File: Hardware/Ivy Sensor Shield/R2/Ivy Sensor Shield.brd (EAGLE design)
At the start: 47.1 x 37.5 mm, 16 parts

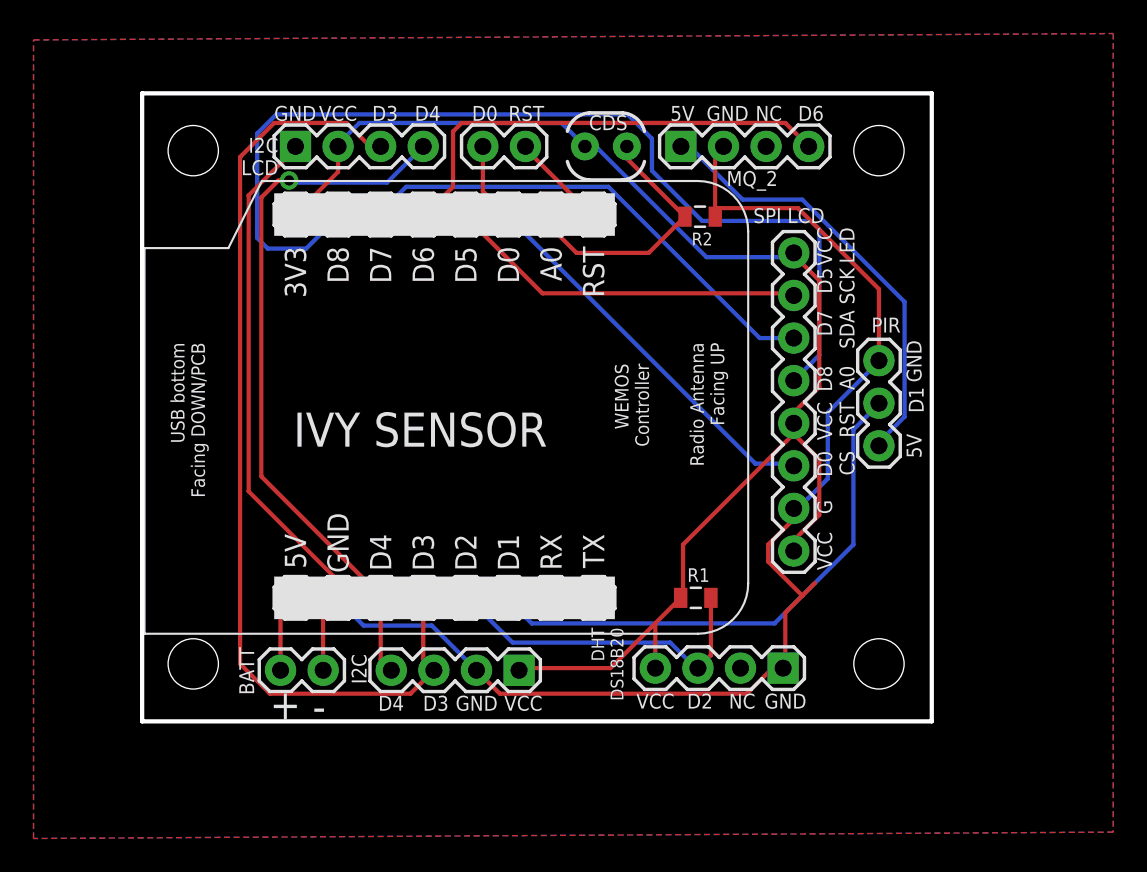
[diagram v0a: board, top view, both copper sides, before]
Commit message: Correct wiring for Ivy Sensor Shield.brd
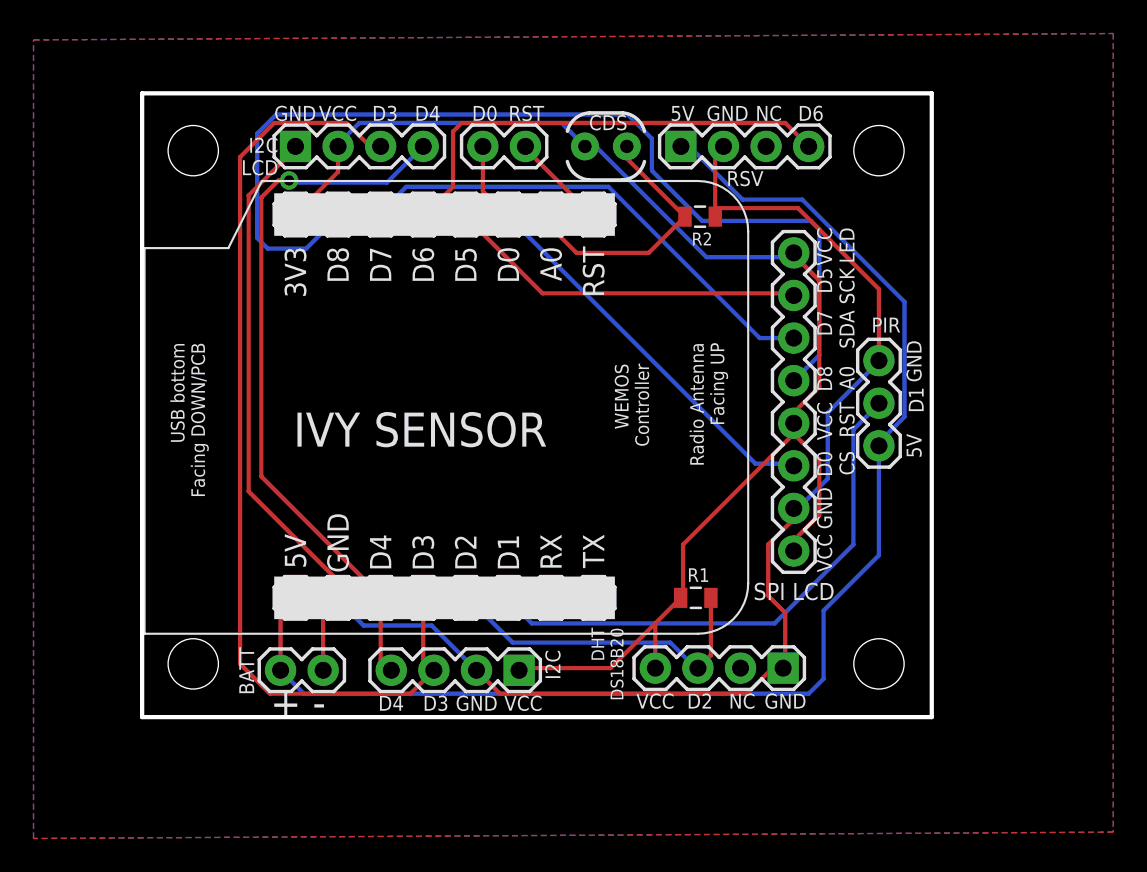
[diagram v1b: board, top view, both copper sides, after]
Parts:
- renumbered MQ_2 to RSV
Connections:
- net AOUT renamed NC2
- removed net VIN: PIR.1, RSV.1
- net 5V: now also PIR.1, RSV.1
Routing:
- net 5V: track 4.81 -> 79.8 mm
- net VIN: track 26.4 -> 0.00 mm
- net GND: track 109.0 -> 107.1 mm
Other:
- board size 47.1 x 37.5 mm -> 47.1 x 37.2 mm
- board text removed: "G"
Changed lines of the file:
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@@
 <board>
 <plain>
-<wire x1="26.162" y1="40.767" x2="73.2536" y2="40.767" width="0.254" layer="20"/>
-<wire x1="73.2536" y1="40.767" x2="73.2536" y2="78.222" width="0.254" layer="20"/>
+<wire x1="26.162" y1="41.021" x2="73.2536" y2="41.021" width="0.254" layer="20"/>
+<wire x1="73.2536" y1="41.021" x2="73.2536" y2="78.222" width="0.254" layer="20"/>
 <wire x1="73.2536" y1="78.222" x2="26.162" y2="78.222" width="0.254" layer="20"/>
-<wire x1="26.162" y1="78.222" x2="26.162" y2="40.767" width="0.254" layer="20"/>
+<wire x1="26.162" y1="78.222" x2="26.162" y2="41.021" width="0.254" layer="20"/>
 <text x="47.371" y="77.47" size="0.889" layer="25" font="vector" ratio="15" rot="R180">D0</text>
 <text x="48.006" y="76.581" size="0.889" layer="25" font="vector" ratio="15" rot="SR0">RST</text>
-<text x="62.611" y="70.485" size="0.889" layer="25" font="vector" ratio="15">SPI LCD</text>
+<text x="62.611" y="48.006" size="1.016" layer="25" font="vector" ratio="15">SPI LCD</text>
 <text x="34.29" y="75.565" size="0.889" layer="25" font="vector" ratio="15" rot="R180">I2C
 LCD</text>
-<text x="33.782" y="40.894" size="1.778" layer="25" font="vector" ratio="15">+</text>
-<text x="36.322" y="40.767" size="1.778" layer="25" font="vector" ratio="15">-</text>
+<text x="33.8074" y="40.9702" size="1.778" layer="25" font="vector" ratio="15">+</text>
+<text x="36.322" y="41.021" size="1.778" layer="25" font="vector" ratio="15">-</text>
 <text x="41.783" y="42.291" size="0.889" layer="25" font="vector" ratio="15" rot="R180">D4</text>
 <text x="44.45" y="42.291" size="0.889" layer="25" font="vector" ratio="15" rot="R180">D3</text>
@@
 <text x="66.421" y="56.896" size="0.889" layer="25" font="vector" ratio="15" rot="R270">D0
 CS</text>
-<text x="66.421" y="53.975" size="0.889" layer="25" font="vector" ratio="15" rot="R270">G</text>
-<text x="66.421" y="52.07" size="0.889" layer="25" font="vector" ratio="15" rot="R270">VCC</text>
+<text x="66.421" y="54.737" size="0.889" layer="25" font="vector" ratio="15" rot="R270">GND</text>
+<text x="66.421" y="51.943" size="0.889" layer="25" font="vector" ratio="15" rot="R270">VCC</text>
 <text x="35.179" y="57.15" size="2.032" layer="25" font="vector" ratio="15">IVY SENSOR</text>
 <text x="52.832" y="59.436" size="2.032" layer="26" font="vector" ratio="15" rot="MR0">IVY SENSOR</text>
@@
 <attribute name="VALUE" x="50.292" y="78.232" size="1.27" layer="27" rot="R180"/>
 </element>
-<element name="MQ_2" library="SparkFun-Connectors" package="1X04" value="" x="58.293" y="75.057" smashed="yes">
+<element name="RSV" library="SparkFun-Connectors" package="1X04" value="" x="58.293" y="75.057" smashed="yes">
 <attribute name="NAME" x="61.0108" y="72.6948" size="0.889" layer="25" font="vector" ratio="15"/>
 <attribute name="VALUE" x="57.023" y="71.882" size="1.27" layer="27"/>
@@
 </element>
 <element name="I2C" library="SparkFun-Connectors" package="1X04" value="I2C" x="48.641" y="43.815" smashed="yes" rot="R180">
-<attribute name="NAME" x="38.6588" y="44.7802" size="0.889" layer="25" font="vector" ratio="15" rot="R270"/>
+<attribute name="NAME" x="50.2158" y="45.0342" size="0.889" layer="25" font="vector" ratio="15" rot="R270"/>
 <attribute name="VALUE" x="49.911" y="46.99" size="1.27" layer="27" rot="R180" display="off"/>
 </element>
@@
 <contactref element="PIR" pad="3"/>
 <contactref element="DHT_DS18B20" pad="1"/>
-<contactref element="MQ_2" pad="2"/>
+<contactref element="RSV" pad="2"/>
 <contactref element="R2" pad="2"/>
 <contactref element="I2C" pad="2"/>
@@
 <wire x1="60.336" y1="74.56" x2="60.833" y2="75.057" width="0.254" layer="1"/>
 <wire x1="64.516" y1="47.244" x2="64.516" y2="43.942" width="0.254" layer="1"/>
-<wire x1="66.294" y1="49.022" x2="65.532" y2="48.26" width="0.254" layer="1"/>
-<wire x1="65.532" y1="48.26" x2="64.516" y2="47.244" width="0.254" layer="1"/>
 <wire x1="64.516" y1="43.942" x2="64.389" y2="43.942" width="0.254" layer="1"/>
 <wire x1="65.278" y1="71.374" x2="60.452" y2="71.374" width="0.254" layer="1"/>
@@
 <wire x1="65.024" y1="52.832" x2="65.024" y2="53.467" width="0.254" layer="1"/>
 <wire x1="63.5" y1="51.308" x2="65.024" y2="52.832" width="0.254" layer="1"/>
-<wire x1="63.5" y1="50.292" x2="63.5" y2="51.308" width="0.254" layer="1"/>
-<wire x1="65.532" y1="48.26" x2="63.5" y2="50.292" width="0.254" layer="1"/>
 <wire x1="70.104" y1="62.23" x2="67.056" y2="59.182" width="0.254" layer="16"/>
 <wire x1="70.104" y1="62.23" x2="70.104" y2="62.2808" width="0.254" layer="16"/>
@@
 <wire x1="43.434" y1="46.482" x2="46.101" y2="43.815" width="0.254" layer="16"/>
 <wire x1="47.498" y1="42.418" x2="46.101" y2="43.815" width="0.254" layer="1"/>
+<wire x1="63.5" y1="51.308" x2="63.5" y2="48.26" width="0.254" layer="1"/>
+<wire x1="63.5" y1="48.26" x2="64.516" y2="47.244" width="0.254" layer="1"/>
 </signal>
 <signal name="N$2">
@@
 <wire x1="49.022" y1="74.93" x2="53.086" y2="70.866" width="0.254" layer="1"/>
 </signal>
-<signal name="VIN">
-<contactref element="PIR" pad="1"/>
-<contactref element="MQ_2" pad="1"/>
-<wire x1="58.928" y1="74.93" x2="58.42" y2="74.93" width="0.254" layer="16"/>
-<wire x1="61.976" y1="71.882" x2="58.928" y2="74.93" width="0.254" layer="16"/>
-<wire x1="65.532" y1="71.882" x2="61.976" y2="71.882" width="0.254" layer="16"/>
-<wire x1="71.628" y1="65.786" x2="65.532" y2="71.882" width="0.254" layer="16"/>
-<wire x1="71.628" y1="58.928" x2="71.628" y2="65.786" width="0.254" layer="16"/>
-<wire x1="70.104" y1="57.404" x2="71.628" y2="58.928" width="0.254" layer="16"/>
-<wire x1="58.42" y1="74.93" x2="58.293" y2="75.057" width="0.254" layer="16"/>
-<wire x1="70.104" y1="57.404" x2="70.104" y2="57.2008" width="0.254" layer="16"/>
-</signal>
 <signal name="NC">
 <contactref element="DHT_DS18B20" pad="2"/>
 </signal>
-<signal name="AOUT">
-<contactref element="MQ_2" pad="3"/>
+<signal name="NC2">
+<contactref element="RSV" pad="3"/>
 </signal>
 <signal name="D0">
@@
 <contactref element="U$2" pad="5V"/>
 <wire x1="34.417" y1="47.371" x2="35.306" y2="48.26" width="0.254" layer="1"/>
+<contactref element="PIR" pad="1"/>
+<contactref element="RSV" pad="1"/>
+<wire x1="58.928" y1="74.93" x2="58.42" y2="74.93" width="0.254" layer="16"/>
+<wire x1="61.976" y1="71.882" x2="58.928" y2="74.93" width="0.254" layer="16"/>
+<wire x1="65.532" y1="71.882" x2="61.976" y2="71.882" width="0.254" layer="16"/>
+<wire x1="71.628" y1="65.786" x2="65.532" y2="71.882" width="0.254" layer="16"/>
+<wire x1="71.628" y1="58.928" x2="71.628" y2="65.786" width="0.254" layer="16"/>
+<wire x1="70.104" y1="57.404" x2="71.628" y2="58.928" width="0.254" layer="16"/>
+<wire x1="58.42" y1="74.93" x2="58.293" y2="75.057" width="0.254" layer="16"/>
+<wire x1="70.104" y1="57.404" x2="70.104" y2="57.2008" width="0.254" layer="16"/>
+<wire x1="70.104" y1="50.673" x2="70.104" y2="57.2008" width="0.254" layer="16"/>
+<wire x1="35.814" y1="42.418" x2="65.913" y2="42.418" width="0.254" layer="16"/>
+<wire x1="34.417" y1="43.815" x2="35.814" y2="42.418" width="0.254" layer="16"/>
+<wire x1="65.913" y1="42.418" x2="66.802" y2="43.307" width="0.254" layer="16"/>
+<wire x1="66.802" y1="43.307" x2="66.802" y2="47.371" width="0.254" layer="16"/>
+<wire x1="66.802" y1="47.371" x2="70.104" y2="50.673" width="0.254" layer="16"/>
 </signal>
 <signal name="D8">
@@
 </signal>
 <signal name="D6">
-<contactref element="MQ_2" pad="4"/>
+<contactref element="RSV" pad="4"/>
 <wire x1="64.516" y1="76.454" x2="45.212" y2="76.454" width="0.254" layer="1"/>
 <wire x1="65.913" y1="75.057" x2="64.516" y2="76.454" width="0.254" layer="1"/>
